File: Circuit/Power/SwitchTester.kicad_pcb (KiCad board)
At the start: 2 copper layers, 53.3 x 17.8 mm, 14 parts, among them J1 12V Power, J2 As Control, J3 As Starter, J4 As Capacitor, J5 As Coil, SW1 SW_SPDT

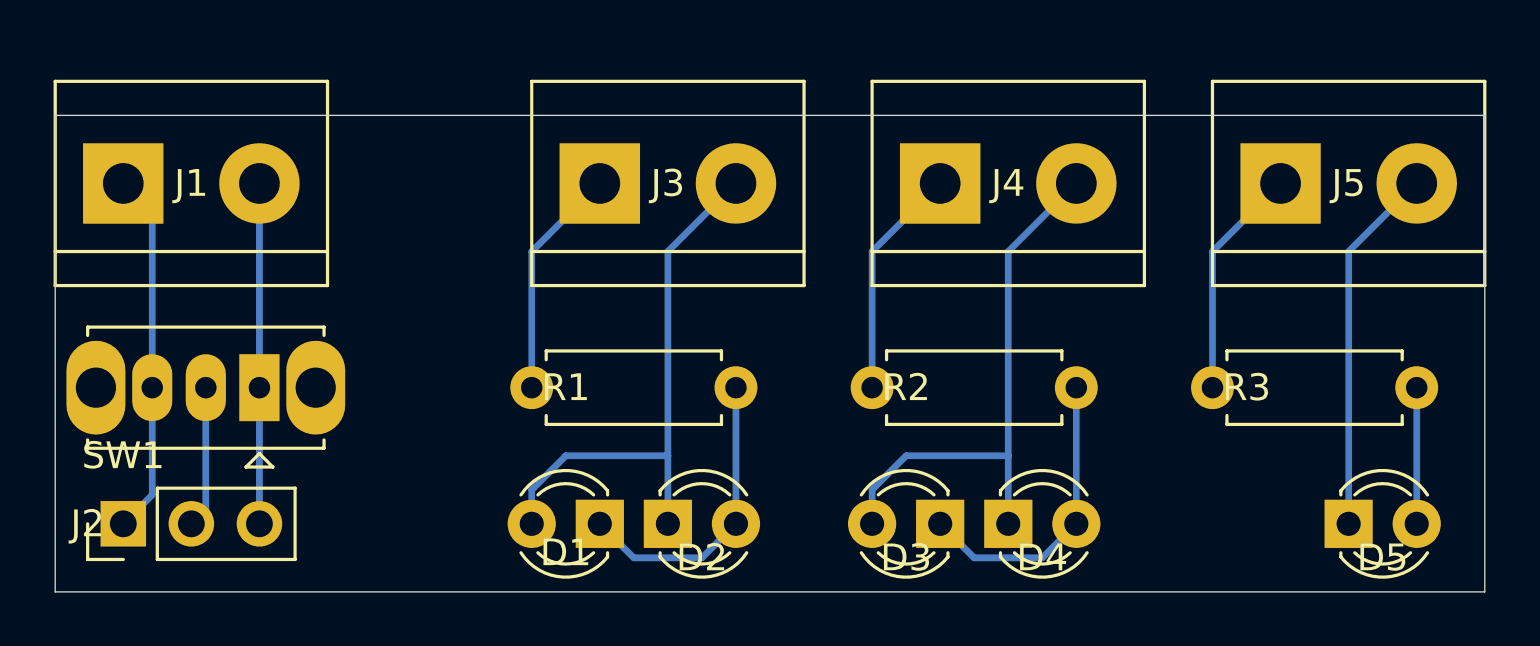
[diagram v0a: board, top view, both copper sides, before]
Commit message: [Circuit] Optimize the switch tester's PCB
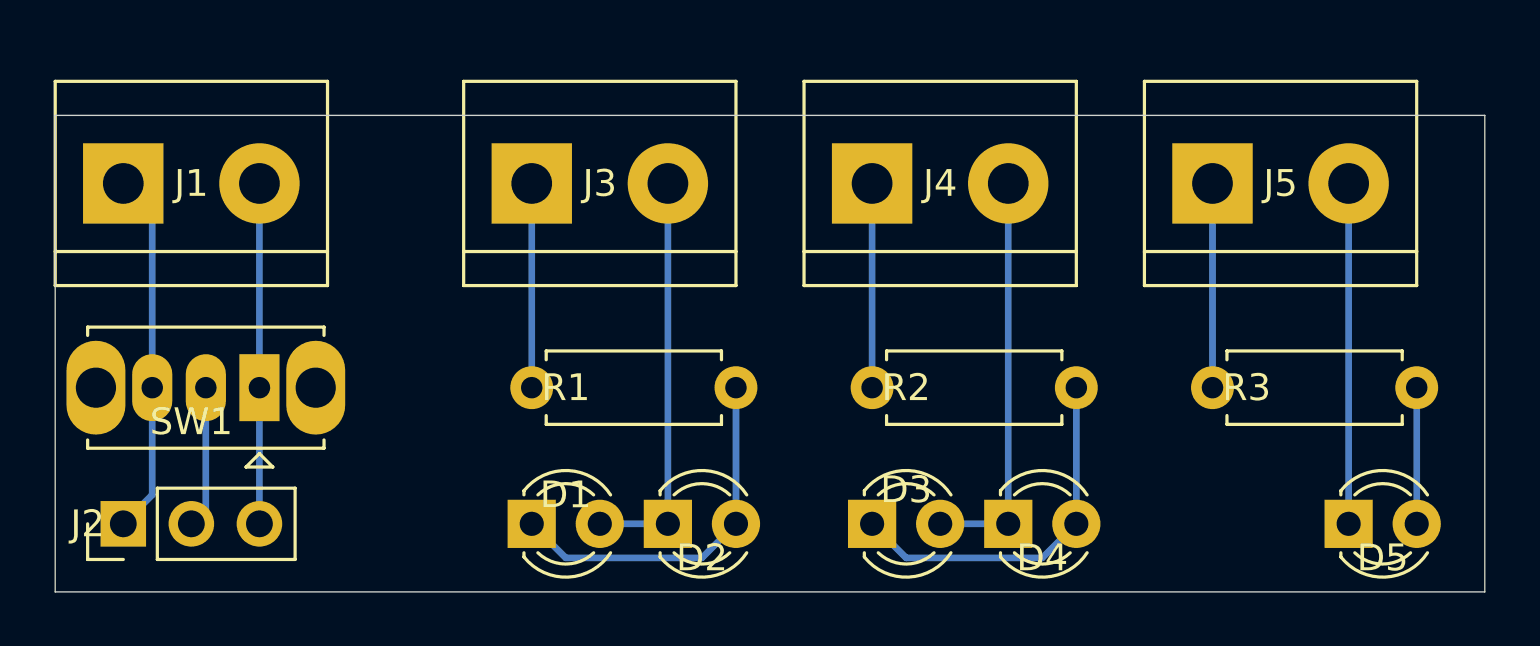
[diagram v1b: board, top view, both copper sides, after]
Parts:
- moved J5 2.54 mm to (124.5, 76.2)
- moved D1 2.54 mm to (99.1, 88.9), turned to 0 degrees
- moved D3 2.54 mm to (111.8, 88.9), turned to 0 degrees
- moved J3 2.54 mm to (99.1, 76.2)
- moved J4 2.54 mm to (111.8, 76.2)
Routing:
- net Net-(D1-Pad2): track 20.6 -> 15.2 mm
- net Net-(D3-Pad2): track 20.6 -> 15.2 mm
- net Net-(D1-Pad1): track 11.2 -> 13.8 mm
- net Net-(D3-Pad1): track 11.2 -> 13.8 mm
- net Net-(D5-Pad1): track 13.8 -> 12.7 mm
- net Net-(J5-Pad1): track 8.67 -> 7.62 mm
- net Net-(J4-Pad1): track 8.67 -> 7.62 mm
- net Net-(J3-Pad1): track 8.67 -> 7.62 mm
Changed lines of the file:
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@@
     (thickness 1.6)
     (drawings 4)
-    (tracks 37)
+    (tracks 25)
     (zones 0)
     (modules 14)
@@
     (descr "CuK miniature slide switch, OS series, SPDT, https://www.ckswitches.com/media/1428/os.pdf")
     (tags "switch SPDT")
-    (fp_text reference SW1 (at 5.08 -2.54) (layer F.SilkS)
-      (effects (font (size 1 1) (thickness 0.15)))
-    )
-    (fp_text value SW_SPDT (at 2 2.54) (layer F.Fab)
+    (fp_text reference SW1 (at 2.54 -1.27) (layer F.SilkS)
+      (effects (font (size 1 1) (thickness 0.15)))
+    )
+    (fp_text value SW_SPDT (at 2 1) (layer F.Fab)
       (effects (font (size 1 1) (thickness 0.15)))
     )
@@
     (fp_line (start 7.45 -2.4) (end 7.45 2.4) (layer B.CrtYd) (width 0.05))
     (fp_line (start -3.45 -2.4) (end 7.45 -2.4) (layer B.CrtYd) (width 0.05))
-    (fp_text user %R (at 5.08 -2.54) (layer F.Fab)
+    (fp_text user %R (at 2.54 -1.27) (layer F.Fab)
       (effects (font (size 1 1) (thickness 0.15)))
     )
@@
   )
   (module TerminalBlock:TerminalBlock_bornier-2_P5.08mm (layer F.Cu)
-    (at 127 76.2)
+    (at 124.46 76.2)
     (descr "simple 2-pin terminal block, pitch 5.08mm, revamped version of bornier2")
     (tags "terminal block bornier2")
@@
   )
   (module TerminalBlock:TerminalBlock_bornier-2_P5.08mm (layer F.Cu)
-    (at 114.3 76.2)
+    (at 111.76 76.2)
     (descr "simple 2-pin terminal block, pitch 5.08mm, revamped version of bornier2")
     (tags "terminal block bornier2")
@@
   )
   (module TerminalBlock:TerminalBlock_bornier-2_P5.08mm (layer F.Cu)
-    (at 101.6 76.2)
+    (at 99.06 76.2)
     (descr "simple 2-pin terminal block, pitch 5.08mm, revamped version of bornier2")
     (tags "terminal block bornier2")
@@
   )
   (module LED_THT:LED_D3.0mm_FlatTop (layer F.Cu)
-    (at 114.3 88.9 180)
+    (at 111.76 88.9)
     (descr "LED, Round, FlatTop, diameter 3.0mm, 2 pins, http://www.kingbright.com/attachments/file/psearch/000/00/00/L-47XEC(Ver.9A).pdf")
     (tags "LED Round FlatTop diameter 3.0mm 2 pins")
@@
     (fp_arc (start 1.27 0) (end -0.29 -1.235516) (angle 108.8) (layer F.SilkS) (width 0.12))
     (fp_arc (start 1.27 0) (end -0.23 -1.16619) (angle 284.3) (layer F.Fab) (width 0.1))
-    (pad 2 thru_hole circle (at 2.54 0 180) (size 1.8 1.8) (drill 0.9) (layers *.Cu *.Mask)
+    (pad 2 thru_hole circle (at 2.54 0) (size 1.8 1.8) (drill 0.9) (layers *.Cu *.Mask)
       (net 3 "Net-(D3-Pad2)"))
-    (pad 1 thru_hole rect (at 0 0 180) (size 1.8 1.8) (drill 0.9) (layers *.Cu *.Mask)
+    (pad 1 thru_hole rect (at 0 0) (size 1.8 1.8) (drill 0.9) (layers *.Cu *.Mask)
       (net 4 "Net-(D3-Pad1)"))
     (model ${KISYS3DMOD}/LED_THT.3dshapes/LED_D3.0mm_FlatTop.wrl
@@
   )
   (module LED_THT:LED_D3.0mm_FlatTop (layer F.Cu)
-    (at 101.6 88.9 180)
+    (at 99.06 88.9)
     (descr "LED, Round, FlatTop, diameter 3.0mm, 2 pins, http://www.kingbright.com/attachments/file/psearch/000/00/00/L-47XEC(Ver.9A).pdf")
     (tags "LED Round FlatTop diameter 3.0mm 2 pins")
@@
     (fp_arc (start 1.27 0) (end -0.29 -1.235516) (angle 108.8) (layer F.SilkS) (width 0.12))
     (fp_arc (start 1.27 0) (end -0.23 -1.16619) (angle 284.3) (layer F.Fab) (width 0.1))
-    (pad 2 thru_hole circle (at 2.54 0 180) (size 1.8 1.8) (drill 0.9) (layers *.Cu *.Mask)
+    (pad 2 thru_hole circle (at 2.54 0) (size 1.8 1.8) (drill 0.9) (layers *.Cu *.Mask)
       (net 1 "Net-(D1-Pad2)"))
-    (pad 1 thru_hole rect (at 0 0 180) (size 1.8 1.8) (drill 0.9) (layers *.Cu *.Mask)
+    (pad 1 thru_hole rect (at 0 0) (size 1.8 1.8) (drill 0.9) (layers *.Cu *.Mask)
       (net 2 "Net-(D1-Pad1)"))
     (model ${KISYS3DMOD}/LED_THT.3dshapes/LED_D3.0mm_FlatTop.wrl
@@
   (gr_line (start 134.62 73.66) (end 134.62 91.44) (layer Edge.Cuts) (width 0.05))
   (gr_line (start 81.28 73.66) (end 134.62 73.66) (layer Edge.Cuts) (width 0.05))
-  (segment (start 104.14 78.74) (end 106.68 76.2) (width 0.25) (layer B.Cu) (net 1) (status 20))
-  (segment (start 99.06 88.9) (end 99.06 87.63) (width 0.25) (layer B.Cu) (net 1) (status 10))
-  (segment (start 99.06 87.63) (end 100.33 86.36) (width 0.25) (layer B.Cu) (net 1))
-  (segment (start 100.33 86.36) (end 104.14 86.36) (width 0.25) (layer B.Cu) (net 1))
-  (segment (start 104.14 88.9) (end 104.14 86.36) (width 0.25) (layer B.Cu) (net 1) (status 10))
-  (segment (start 104.14 86.36) (end 104.14 78.74) (width 0.25) (layer B.Cu) (net 1))
+  (segment (start 104.14 88.9) (end 104.14 76.2) (width 0.25) (layer B.Cu) (net 1) (status 30))
+  (segment (start 101.6 88.9) (end 104.14 88.9) (width 0.25) (layer B.Cu) (net 1) (status 30))
   (segment (start 106.68 83.82) (end 106.68 88.9) (width 0.25) (layer B.Cu) (net 2) (status 30))
-  (segment (start 101.6 88.9) (end 102.87 90.17) (width 0.25) (layer B.Cu) (net 2))
-  (segment (start 102.87 90.17) (end 105.41 90.17) (width 0.25) (layer B.Cu) (net 2))
-  (segment (start 105.41 90.17) (end 106.68 88.9) (width 0.25) (layer B.Cu) (net 2))
-  (segment (start 119.38 76.2) (end 116.84 78.74) (width 0.25) (layer B.Cu) (net 3))
-  (segment (start 111.76 88.9) (end 111.76 87.63) (width 0.25) (layer B.Cu) (net 3))
-  (segment (start 111.76 87.63) (end 113.03 86.36) (width 0.25) (layer B.Cu) (net 3))
-  (segment (start 113.03 86.36) (end 116.84 86.36) (width 0.25) (layer B.Cu) (net 3))
-  (segment (start 116.84 78.74) (end 116.84 86.36) (width 0.25) (layer B.Cu) (net 3))
-  (segment (start 116.84 86.36) (end 116.84 88.9) (width 0.25) (layer B.Cu) (net 3))
-  (segment (start 119.38 83.82) (end 119.38 88.9) (width 0.25) (layer B.Cu) (net 4))
-  (segment (start 114.3 88.9) (end 115.57 90.17) (width 0.25) (layer B.Cu) (net 4))
-  (segment (start 115.57 90.17) (end 118.11 90.17) (width 0.25) (layer B.Cu) (net 4))
-  (segment (start 118.11 90.17) (end 119.38 88.9) (width 0.25) (layer B.Cu) (net 4))
-  (segment (start 132.08 83.82) (end 132.08 88.9) (width 0.25) (layer B.Cu) (net 5))
-  (segment (start 129.54 78.74) (end 132.08 76.2) (width 0.25) (layer B.Cu) (net 6))
-  (segment (start 129.54 88.9) (end 129.54 78.74) (width 0.25) (layer B.Cu) (net 6))
-  (segment (start 88.9 76.2) (end 88.9 83.82) (width 0.25) (layer B.Cu) (net 12) (status 30))
-  (segment (start 88.9 83.82) (end 88.9 88.9) (width 0.25) (layer B.Cu) (net 12) (status 30))
+  (segment (start 105.41 90.17) (end 106.68 88.9) (width 0.25) (layer B.Cu) (net 2) (status 20))
+  (segment (start 100.33 90.17) (end 99.06 88.9) (width 0.25) (layer B.Cu) (net 2) (status 20))
+  (segment (start 105.41 90.17) (end 100.33 90.17) (width 0.25) (layer B.Cu) (net 2))
+  (segment (start 116.84 76.2) (end 116.84 88.9) (width 0.25) (layer B.Cu) (net 3) (status 30))
+  (segment (start 116.84 88.9) (end 114.3 88.9) (width 0.25) (layer B.Cu) (net 3) (status 30))
+  (segment (start 119.38 83.82) (end 119.38 88.9) (width 0.25) (layer B.Cu) (net 4) (status 30))
+  (segment (start 113.03 90.17) (end 111.76 88.9) (width 0.25) (layer B.Cu) (net 4) (status 20))
+  (segment (start 119.38 88.9) (end 118.11 90.17) (width 0.25) (layer B.Cu) (net 4) (status 10))
+  (segment (start 118.11 90.17) (end 113.03 90.17) (width 0.25) (layer B.Cu) (net 4))
+  (segment (start 132.08 83.82) (end 132.08 88.9) (width 0.25) (layer B.Cu) (net 5) (status 30))
+  (segment (start 129.54 88.9) (end 129.54 76.2) (width 0.25) (layer B.Cu) (net 6) (status 30))
   (segment (start 84.9 87.82) (end 83.82 88.9) (width 0.25) (layer B.Cu) (net 7) (status 20))
   (segment (start 84.9 83.82) (end 84.9 87.82) (width 0.25) (layer B.Cu) (net 7) (status 10))
@@
   (segment (start 86.9 88.36) (end 86.36 88.9) (width 0.25) (layer B.Cu) (net 8) (status 30))
   (segment (start 86.9 83.82) (end 86.9 88.36) (width 0.25) (layer B.Cu) (net 8) (status 30))
-  (segment (start 99.06 78.74) (end 101.6 76.2) (width 0.25) (layer B.Cu) (net 9) (status 20))
-  (segment (start 99.06 83.82) (end 99.06 78.74) (width 0.25) (layer B.Cu) (net 9) (status 10))
-  (segment (start 111.76 78.74) (end 114.3 76.2) (width 0.25) (layer B.Cu) (net 10))
-  (segment (start 111.76 83.82) (end 111.76 78.74) (width 0.25) (layer B.Cu) (net 10))
-  (segment (start 124.46 78.74) (end 127 76.2) (width 0.25) (layer B.Cu) (net 11))
-  (segment (start 124.46 83.82) (end 124.46 78.74) (width 0.25) (layer B.Cu) (net 11))
+  (segment (start 99.06 83.82) (end 99.06 76.2) (width 0.25) (layer B.Cu) (net 9) (status 30))
+  (segment (start 111.76 83.82) (end 111.76 76.2) (width 0.25) (layer B.Cu) (net 10) (status 30))
+  (segment (start 124.46 83.82) (end 124.46 76.2) (width 0.25) (layer B.Cu) (net 11) (status 30))
+  (segment (start 88.9 76.2) (end 88.9 83.82) (width 0.25) (layer B.Cu) (net 12) (status 30))
+  (segment (start 88.9 83.82) (end 88.9 88.9) (width 0.25) (layer B.Cu) (net 12) (status 30))
 )

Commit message: [Circuit] Optimizations on PCB layouts
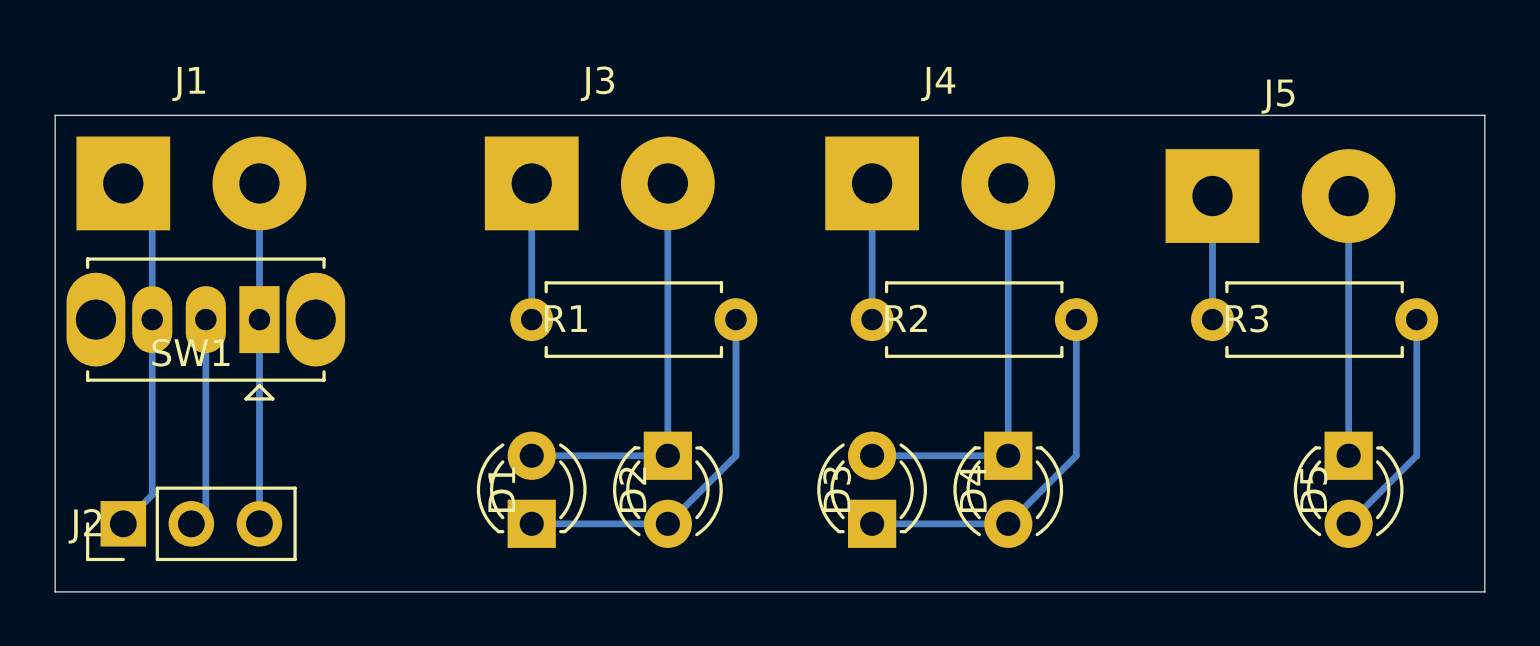
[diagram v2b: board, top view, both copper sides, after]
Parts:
- J1, J3, J4, J5: footprint TerminalBlock:TerminalBlock_bornier-2_P5.08mm -> Connector_Wire:SolderWirePad_1x02_P5.08mm_Drill1.5mm
- moved D2 2.54 mm to (104.1, 86.4), turned to 270 degrees
- moved D4 2.54 mm to (116.8, 86.4), turned to 270 degrees
- moved D5 2.54 mm to (129.5, 86.4), turned to 270 degrees
- moved R1 2.54 mm to (99.1, 81.3)
- moved R2 2.54 mm to (111.8, 81.3)
- moved R3 2.54 mm to (124.5, 81.3)
- moved SW1 2.54 mm to (88.9, 81.3)
- moved J5 0.47 mm to (124.5, 76.7)
- turned D1 to 90 degrees
- turned D3 to 90 degrees
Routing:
- net Net-(D5-Pad2): track 5.08 -> 8.67 mm
- net Net-(D5-Pad1): track 12.7 -> 10.2 mm
- net Net-(J5-Pad1): track 7.62 -> 5.08 mm
- net Net-(J4-Pad1): track 7.62 -> 5.08 mm
- net Net-(J3-Pad1): track 7.62 -> 5.08 mm
- net Net-(J2-Pad2): track 5.30 -> 7.84 mm
